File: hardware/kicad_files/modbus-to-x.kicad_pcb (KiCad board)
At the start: 4 copper layers, 87.6 x 46.7 mm, 40 parts, among them IC1 ESP32-WROOM-32D_M113DH2800PH3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, J1 615006138421, J4 M50-3140545R, Q1 DSS4160U-7, Q2 DSS4160U-7, SW1 SW_Wuerth_450301014042, SW4 3983, U1 LM2596S-3.3, U3 MAX3485

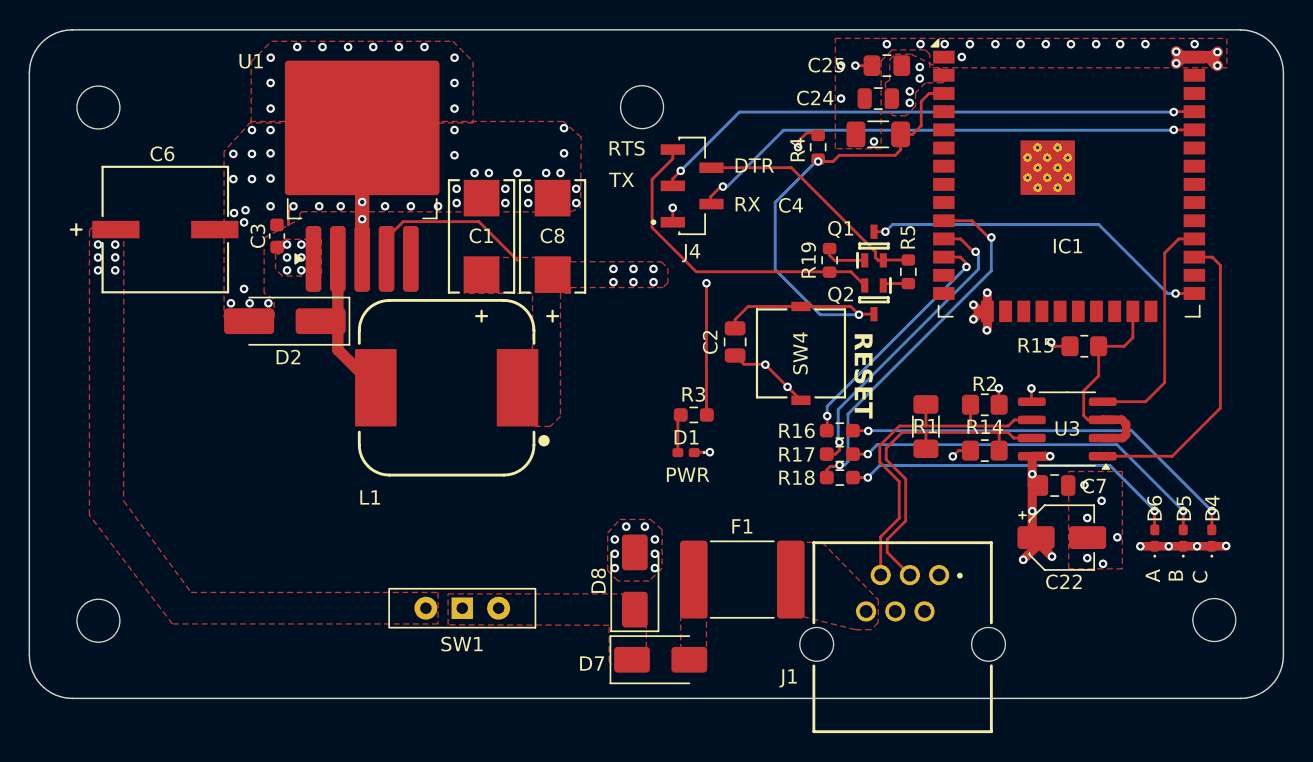
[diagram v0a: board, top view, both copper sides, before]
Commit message: - Added Micro USB port - Added header for OpenLog - Minor silkscreen updates - New buck conv. inductor improving cost
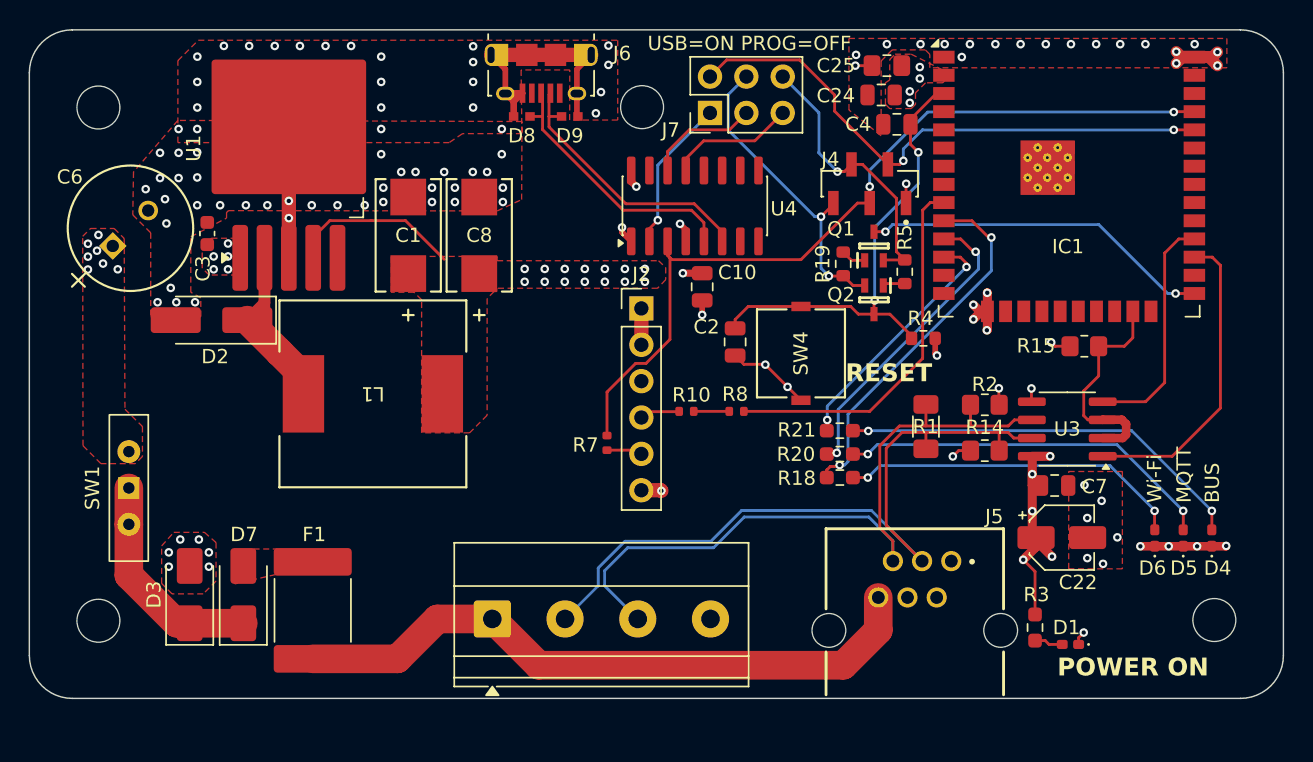
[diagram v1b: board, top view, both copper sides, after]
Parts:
- removed J1: 615006138421, project_footprints:RJ12_615006138421
- removed R16, R17: 2K, Resistor_SMD:R_0603_1608Metric_Pad0.98x0.95mm_HandSolder
- added C10: 0.1uF, Capacitor_SMD:C_0805_2012Metric, F.Cu at (91.9, 105.5)
- added D3: SMAJ33A, Diode_SMD:D_SMA, F.Cu at (56.1, 127.0)
- added D9: PESD0402-140, project_footprints:PESD0402-140_LTF, F.Cu at (82.7, 93.5)
- added J2: OpenLog, project_footprints:MBX_PinHeader_1x06_P2.54mm_Vertical, F.Cu at (87.7, 107.0)
- added J3: Screw_Terminal_01x04, TerminalBlock_Phoenix:TerminalBlock_Phoenix_MKDS-1,5-4-5.08_1x04_P5.08mm_Horizontal, F.Cu at (77.2, 128.7)
- added J5: 615006138421, project_footprints:RJ12_615006138421, F.Cu at (106.8, 128.9)
- added J6: Micro USB, project_footprints:AMPHENOL_10118194-0001LF, F.Cu at (80.7, 89.2)
- added J7: USB_ENABLE, Connector_PinHeader_2.54mm:PinHeader_2x03_P2.54mm_Vertical, F.Cu at (92.4, 93.3)
- added R10: 402, project_footprints:MBX_R_0402_1005Metric, F.Cu at (90.8, 114.2)
- added R20: 2K, Resistor_SMD:R_0603_1608Metric_Pad0.98x0.95mm_HandSolder, F.Cu at (101.5, 117.1)
- added R21: 2K, Resistor_SMD:R_0603_1608Metric_Pad0.98x0.95mm_HandSolder, F.Cu at (101.5, 115.5)
- added R7: 402, project_footprints:MBX_R_0402_1005Metric, F.Cu at (85.2, 116.3)
- added R8: 402, project_footprints:MBX_R_0402_1005Metric, F.Cu at (94.3, 114.2)
- added U4: CH340C, Package_SO:SOIC-16_3.9x9.9mm_P1.27mm, F.Cu at (91.4, 99.8)
- C4: footprint Capacitor_SMD:C_1206_3216Metric_Pad1.33x1.80mm_HandSolder -> Capacitor_SMD:C_0805_2012Metric
- C6: footprint project_footprints:25SVPF100M -> project_footprints:ESY107M050AG3AA
- D8: value SMAJ12A -> PESD0402-140; footprint Diode_SMD:D_SMA -> project_footprints:PESD0402-140_LTF
- G***: footprint Modbus To X Graphics:modbus_to_x_logo.kicad_40x40mm_mod -> project_footprints:modbus_to_x_logo_40x40mm
- L1: footprint project_footprints:7447709330 -> project_footprints:IND_BOURNS_SRR1260
- SW1: value SW_Wuerth_450301014042 -> SS12D00G3
- U1: footprint Package_TO_SOT_SMD:TO-263-5_TabPin3 -> project_footprints:TO-263-5_TabPin3_silk_fix
- moved D8 33.4 mm to (79.3, 93.5), turned to 0 degrees
- moved F1 30.1 mm to (64.7, 128.1), turned to -90 degrees
- moved D1 30.0 mm to (117.6, 130.4)
- moved D7 29.5 mm to (59.8, 127.0), turned to 90 degrees
- moved R3 28.1 mm to (115.2, 129.2), turned to -90 degrees
- moved SW1 24.8 mm to (51.9, 119.5), turned to 90 degrees
- moved R4 15.2 mm to (107.3, 109.0), turned to 180 degrees
- moved J4 12.4 mm to (103.6, 98.2), turned to 0 degrees
- moved L1 5.17 mm to (68.9, 112.9), turned to 180 degrees
- moved U1 5.12 mm to (63.0, 95.8)
- moved C1 5.12 mm to (71.4, 101.9)
- moved C8 5.12 mm to (76.3, 101.9)
- moved D2 5.12 mm to (57.6, 107.8)
- moved C3 4.88 mm to (57.3, 101.7)
- moved C6 3.85 mm to (50.7, 102.6), turned to 45 degrees
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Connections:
- D8 pad 1: /V_PROT -> GND
- D8 pad 2: GND -> /D+
- IC1 pad 9: unconnected-(IC1-IO33-Pad9) -> /IO_33
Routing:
- net /V_EXT: track 0.00 -> 45.3 mm
- net /RS485-: track 23.8 -> 52.4 mm
- net GND: track 41.1 -> 68.8 mm, vias 103 -> 110
- net /RS485+: track 24.5 -> 50.9 mm
- net /IO_33: track 0.00 -> 26.1 mm
- net /TX_0: track 38.7 -> 58.4 mm
- net /D-: track 0.00 -> 19.1 mm
- net /D+: track 0.00 -> 18.7 mm
- net /V_PROT: track 0.00 -> 15.5 mm
- net VDD33: track 37.3 -> 52.2 mm, vias 18 -> 28
- net /USB_TXD: track 0.00 -> 10.7 mm, vias 0 -> 1
- net /USB_DTR: track 0.00 -> 8.92 mm
- net Net-(D2-A1): track 10.1 -> 18.7 mm
- net /USB_RTS: track 0.00 -> 7.94 mm
- net /EN: track 39.6 -> 32.7 mm
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- removed copper zone on F.Cu, net /V_EXT
- removed copper zone on F.Cu, net /V_PROT
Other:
- board text added: "BUS"
- board text added: "MQTT"
- board text added: "POWER ON"
- board text added: "USB=ON PROG=OFF"
- board text added: "Wi-Fi"
- board text removed: "A"
- board text removed: "A+"
- board text removed: "B"
- board text removed: "B-"
- board text removed: "C"
- board text removed: "DTR"
- board text removed: "GND"
- board text removed: "NC"
- board text removed: "PWR"
- board text removed: "RTS"
- board text removed: "RX"
- board text removed: "TX"
- board text removed: "VIN"
